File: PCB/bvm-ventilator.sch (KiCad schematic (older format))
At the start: 6 parts, among them U1 IEC_CONNECTOR

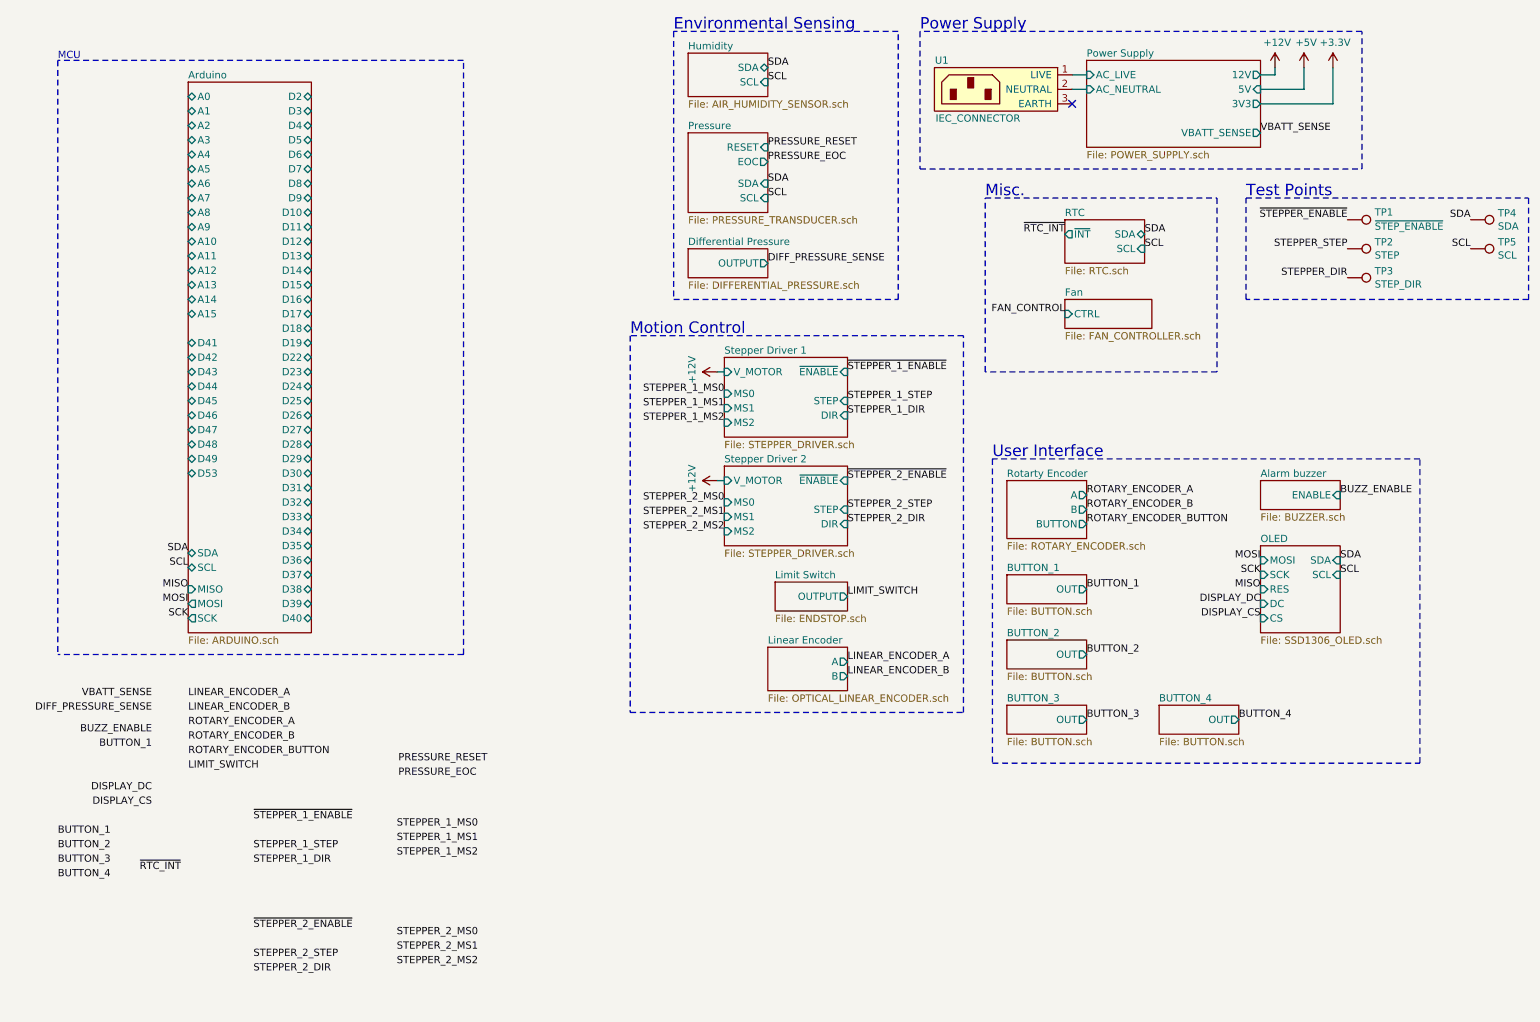
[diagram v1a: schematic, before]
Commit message: Added TFT Display sheet
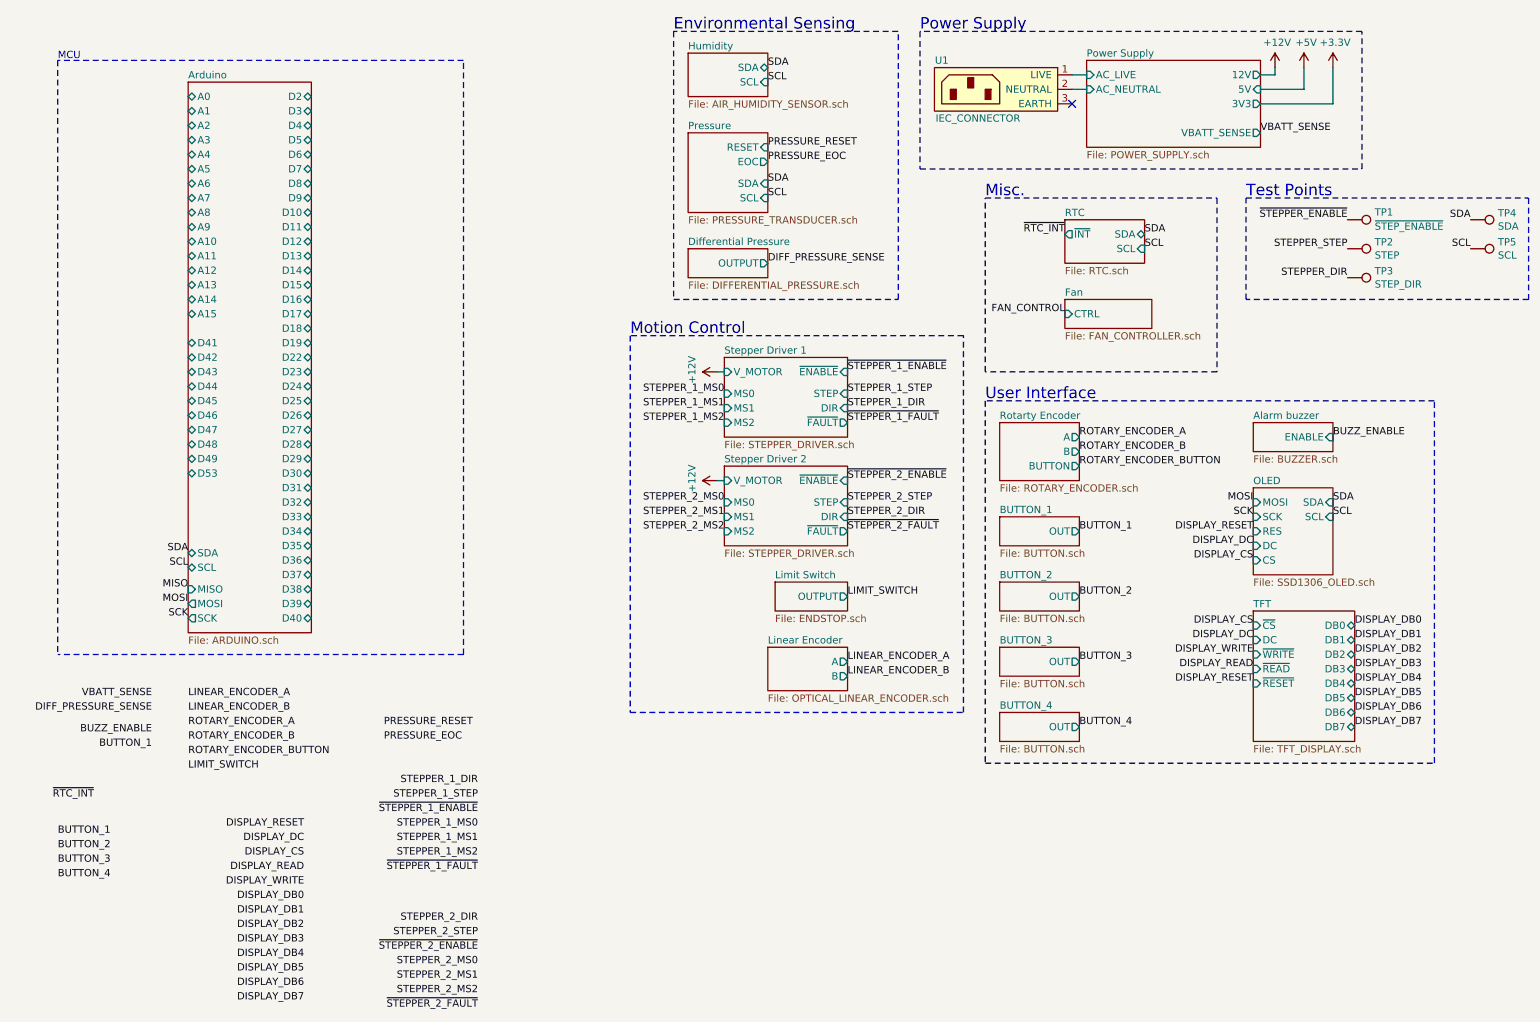
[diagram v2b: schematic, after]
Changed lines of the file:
@@
 $Descr A4 11693 8268
 encoding utf-8
-Sheet 1 26
+Sheet 1 27
 Title "ResQVenT"
 Date ""
@@
 F1 "STEPPER_DRIVER.sch" 50
 F2 "V_MOTOR" I L 5450 3150 50
-F3 "STEP" I R 6300 3350 50
-F4 "DIR" I R 6300 3450 50
+F3 "STEP" I R 6300 3300 50
+F4 "DIR" I R 6300 3400 50
 F5 "~ENABLE" I R 6300 3150 50
 F6 "MS0" I L 5450 3300 50
 F7 "MS1" I L 5450 3400 50
 F8 "MS2" I L 5450 3500 50
-$EndSheet
-$Sheet
-S 9150 3900 550  200
+F9 "~FAULT" O R 6300 3500 50
+$EndSheet
+$Sheet
+S 9100 3500 550  200
 U 5E8EB699
 F0 "Alarm buzzer" 50
 F1 "BUZZER.sch" 50
-F2 "ENABLE" I R 9700 4000 50
-$EndSheet
-$Sheet
-S 9150 4350 550  600
+F2 "ENABLE" I R 9650 3600 50
+$EndSheet
+$Sheet
+S 9100 3950 550  600
 U 5E8F3A13
 F0 "OLED" 50
 F1 "SSD1306_OLED.sch" 50
-F2 "SCL" I R 9700 4550 50
-F3 "SDA" I R 9700 4450 50
-F4 "MOSI" I L 9150 4450 50
-F5 "SCK" I L 9150 4550 50
-F6 "DC" I L 9150 4750 50
-F7 "CS" I L 9150 4850 50
-F8 "RES" I L 9150 4650 50
+F2 "SCL" I R 9650 4150 50
+F3 "SDA" I R 9650 4050 50
+F4 "MOSI" I L 9100 4050 50
+F5 "SCK" I L 9100 4150 50
+F6 "DC" I L 9100 4350 50
+F7 "CS" I L 9100 4450 50
+F8 "RES" I L 9100 4250 50
 $EndSheet
 $Sheet
@@
 F1 "STEPPER_DRIVER.sch" 50
 F2 "V_MOTOR" I L 5450 3900 50
-F3 "STEP" I R 6300 4100 50
-F4 "DIR" I R 6300 4200 50
+F3 "STEP" I R 6300 4050 50
+F4 "DIR" I R 6300 4150 50
 F5 "~ENABLE" I R 6300 3900 50
 F6 "MS0" I L 5450 4050 50
 F7 "MS1" I L 5450 4150 50
 F8 "MS2" I L 5450 4250 50
+F9 "~FAULT" O R 6300 4250 50
 $EndSheet
 $Sheet
@@
 Text Label 1750 4500 2    50   ~ 0
 SCL
-Text Label 9700 4450 0    50   ~ 0
+Text Label 9650 4050 0    50   ~ 0
 SDA
-Text Label 9700 4550 0    50   ~ 0
+Text Label 9650 4150 0    50   ~ 0
 SCL
 Text Label 5750 1850 0    50   ~ 0
@@
 Text Label 8350 2300 0    50   ~ 0
 SCL
-Text Label 6300 3350 0    50   ~ 0
+Text Label 6300 3300 0    50   ~ 0
 STEPPER_1_STEP
-Text Label 6300 3450 0    50   ~ 0
+Text Label 6300 3400 0    50   ~ 0
 STEPPER_1_DIR
-Text Label 6300 4100 0    50   ~ 0
+Text Label 6300 4050 0    50   ~ 0
 STEPPER_2_STEP
-Text Label 6300 4200 0    50   ~ 0
+Text Label 6300 4150 0    50   ~ 0
 STEPPER_2_DIR
-Text Label 9700 4000 0    50   ~ 0
+Text Label 9650 3600 0    50   ~ 0
 BUZZ_ENABLE
-Text Label 1500 5650 2    50   ~ 0
-BUZZ_ENABLE
-Text Label 1750 5900 0    50   ~ 0
-LIMIT_SWITCH
 Text Label 6300 4700 0    50   ~ 0
 LIMIT_SWITCH
@@
 VBATT_SENSE
 $Sheet
-S 7400 3900 550  400
+S 7350 3500 550  400
 U 5E8BEE14
 F0 "Rotarty Encoder" 50
 F1 "ROTARY_ENCODER.sch" 50
-F2 "A" O R 7950 4000 50
-F3 "B" O R 7950 4100 50
-F4 "BUTTON" O R 7950 4200 50
-$EndSheet
-Text Label 7950 4000 0    50   ~ 0
+F2 "A" O R 7900 3600 50
+F3 "B" O R 7900 3700 50
+F4 "BUTTON" O R 7900 3800 50
+$EndSheet
+Text Label 7900 3600 0    50   ~ 0
 ROTARY_ENCODER_A
-Text Label 7950 4100 0    50   ~ 0
+Text Label 7900 3700 0    50   ~ 0
 ROTARY_ENCODER_B
-Text Label 7950 4200 0    50   ~ 0
+Text Label 7900 3800 0    50   ~ 0
 ROTARY_ENCODER_BUTTON
-Text Label 1750 5600 0    50   ~ 0
-ROTARY_ENCODER_A
-Text Label 1750 5700 0    50   ~ 0
-ROTARY_ENCODER_B
-Text Label 1750 5800 0    50   ~ 0
-ROTARY_ENCODER_BUTTON
-$Sheet
-S 7400 4550 550  200
+$Sheet
+S 7350 4150 550  200
 U 5E8CBD7F
 F0 "BUTTON_1" 50
 F1 "BUTTON.sch" 50
-F2 "OUT" O R 7950 4650 50
-$EndSheet
-Text Label 7950 4650 0    50   ~ 0
-BUTTON_1
-Text Label 1500 5750 2    50   ~ 0
+F2 "OUT" O R 7900 4250 50
+$EndSheet
+Text Label 7900 4250 0    50   ~ 0
 BUTTON_1
 Text Label 6300 3150 0    50   ~ 0
@@
 Text Label 6300 5250 0    50   ~ 0
 LINEAR_ENCODER_B
-Text Label 1750 5400 0    50   ~ 0
-LINEAR_ENCODER_A
-Text Label 1750 5500 0    50   ~ 0
-LINEAR_ENCODER_B
 $Sheet
 S 5200 950  550  300
@@
 Text Label 1750 4850 2    50   ~ 0
 SCK
-Text Label 9150 4750 2    50   ~ 0
+Text Label 9100 4350 2    50   ~ 0
 DISPLAY_DC
-Text Label 9150 4850 2    50   ~ 0
+Text Label 9100 4450 2    50   ~ 0
 DISPLAY_CS
-Text Label 9150 4650 2    50   ~ 0
-MISO
-Text Label 9150 4450 2    50   ~ 0
+Text Label 9100 4050 2    50   ~ 0
 MOSI
-Text Label 9150 4550 2    50   ~ 0
+Text Label 9100 4150 2    50   ~ 0
 SCK
 Wire Notes Line
-	7300 3750 7300 5850
-Wire Notes Line
-	7300 5850 10250 5850
-Wire Notes Line
-	10250 5850 10250 3750
-Wire Notes Line
-	10250 3750 7300 3750
+	7250 3350 7250 5850
+Wire Notes Line
+	7250 5850 10350 5850
+Wire Notes Line
+	10350 3350 7250 3350
 Text Notes 4800 2900 0    79   ~ 0
 Motion Control
@@
 Text Notes 5100 800  0    79   ~ 0
 Environmental Sensing
-Text Notes 7300 3750 0    79   ~ 0
+Text Notes 7250 3350 0    79   ~ 0
 User Interface
 Wire Wire Line
@@
 Text Label 7800 2200 2    50   ~ 0
 ~RTC_INT
-Text Label 1700 6600 2    50   ~ 0
+Text Label 1100 6100 2    50   ~ 0
 ~RTC_INT
-Text Label 2200 6450 0    50   ~ 0
-STEPPER_1_STEP
-Text Label 2200 6550 0    50   ~ 0
-STEPPER_1_DIR
-Text Label 2200 7200 0    50   ~ 0
-STEPPER_2_STEP
-Text Label 2200 7300 0    50   ~ 0
-STEPPER_2_DIR
-Text Label 2200 7000 0    50   ~ 0
-~STEPPER_2_ENABLE
-Text Label 2200 6250 0    50   ~ 0
-~STEPPER_1_ENABLE
 Text Label 5450 3300 2    50   ~ 0
 STEPPER_1_MS0
@@
 Text Label 5450 4250 2    50   ~ 0
 STEPPER_2_MS2
-Text Label 3750 6300 2    50   ~ 0
-STEPPER_1_MS0
-Text Label 3750 6400 2    50   ~ 0
-STEPPER_1_MS1
-Text Label 3750 6500 2    50   ~ 0
-STEPPER_1_MS2
-Text Label 3750 7050 2    50   ~ 0
-STEPPER_2_MS0
-Text Label 3750 7150 2    50   ~ 0
-STEPPER_2_MS1
-Text Label 3750 7250 2    50   ~ 0
-STEPPER_2_MS2
 Text Label 5750 1600 0    50   ~ 0
 PRESSURE_RESET
 Text Label 5750 1700 0    50   ~ 0
 PRESSURE_EOC
-Text Label 3200 5850 0    50   ~ 0
-PRESSURE_RESET
-Text Label 3200 5950 0    50   ~ 0
-PRESSURE_EOC
-$Sheet
-S 7400 5000 550  200
+$Sheet
+S 7350 4600 550  200
 U 5E96853E
 F0 "BUTTON_2" 50
 F1 "BUTTON.sch" 50
-F2 "OUT" O R 7950 5100 50
-$EndSheet
-Text Label 7950 5100 0    50   ~ 0
+F2 "OUT" O R 7900 4700 50
+$EndSheet
+Text Label 7900 4700 0    50   ~ 0
 BUTTON_2
 $Sheet
-S 7400 5450 550  200
+S 7350 5050 550  200
 U 5E968934
 F0 "BUTTON_3" 50
 F1 "BUTTON.sch" 50
-F2 "OUT" O R 7950 5550 50
-$EndSheet
-Text Label 7950 5550 0    50   ~ 0
+F2 "OUT" O R 7900 5150 50
+$EndSheet
+Text Label 7900 5150 0    50   ~ 0
 BUTTON_3
 $Sheet
-S 8450 5450 550  200
+S 7350 5500 550  200
 U 5E968D0C
 F0 "BUTTON_4" 50
 F1 "BUTTON.sch" 50
-F2 "OUT" O R 9000 5550 50
-$EndSheet
-Text Label 9000 5550 0    50   ~ 0
+F2 "OUT" O R 7900 5600 50
+$EndSheet
+Text Label 7900 5600 0    50   ~ 0
 BUTTON_4
 Text Label 850  6450 0    50   ~ 0
@@
 Text Label 850  6350 0    50   ~ 0
 BUTTON_1
-Text Label 1500 6050 2    50   ~ 0
+Text Label 2550 6400 2    50   ~ 0
 DISPLAY_DC
-Text Label 1500 6150 2    50   ~ 0
+Text Label 2550 6500 2    50   ~ 0
 DISPLAY_CS
+Text Label 6300 3500 0    50   ~ 0
+~STEPPER_1_FAULT
+Text Label 6300 4250 0    50   ~ 0
+~STEPPER_2_FAULT
+Text Label 1500 5650 2    50   ~ 0
+BUZZ_ENABLE
+Text Label 1500 5750 2    50   ~ 0
+BUTTON_1
+Text Label 1750 5500 0    50   ~ 0
+LINEAR_ENCODER_B
+Text Label 1750 5400 0    50   ~ 0
+LINEAR_ENCODER_A
+Text Label 1750 5800 0    50   ~ 0
+ROTARY_ENCODER_BUTTON
+Text Label 1750 5700 0    50   ~ 0
+ROTARY_ENCODER_B
+Text Label 1750 5600 0    50   ~ 0
+ROTARY_ENCODER_A
+Text Label 1750 5900 0    50   ~ 0
+LIMIT_SWITCH
+Text Label 3100 5700 0    50   ~ 0
+PRESSURE_EOC
+Text Label 3100 5600 0    50   ~ 0
+PRESSURE_RESET
+Text Label 3750 6600 2    50   ~ 0
+~STEPPER_1_FAULT
+Text Label 3750 6500 2    50   ~ 0
+STEPPER_1_MS2
+Text Label 3750 6400 2    50   ~ 0
+STEPPER_1_MS1
+Text Label 3750 6300 2    50   ~ 0
+STEPPER_1_MS0
+Text Label 3750 6200 2    50   ~ 0
+~STEPPER_1_ENABLE
+Text Label 3750 6000 2    50   ~ 0
+STEPPER_1_DIR
+Text Label 3750 6100 2    50   ~ 0
+STEPPER_1_STEP
+Text Label 3750 7050 2    50   ~ 0
+STEPPER_2_STEP
+Text Label 3750 6950 2    50   ~ 0
+STEPPER_2_DIR
+Text Label 3750 7550 2    50   ~ 0
+~STEPPER_2_FAULT
+Text Label 3750 7450 2    50   ~ 0
+STEPPER_2_MS2
+Text Label 3750 7350 2    50   ~ 0
+STEPPER_2_MS1
+Text Label 3750 7250 2    50   ~ 0
+STEPPER_2_MS0
+Text Label 3750 7150 2    50   ~ 0
+~STEPPER_2_ENABLE
+Text Label 9100 4250 2    50   ~ 0
+DISPLAY_RESET
+$Sheet
+S 9100 4800 700  900
+U 5E97D98A
+F0 "TFT" 50
+F1 "TFT_DISPLAY.sch" 50
+F2 "~CS" I L 9100 4900 50
+F3 "DC" I L 9100 5000 50
+F4 "~WRITE" I L 9100 5100 50
+F5 "~READ" I L 9100 5200 50
+F6 "~RESET" I L 9100 5300 50
+F7 "DB0" B R 9800 4900 50
+F8 "DB1" B R 9800 5000 50
+F9 "DB2" B R 9800 5100 50
+F10 "DB3" B R 9800 5200 50
+F11 "DB4" B R 9800 5300 50
+F12 "DB5" B R 9800 5400 50
+F13 "DB6" B R 9800 5500 50
+F14 "DB7" B R 9800 5600 50
+$EndSheet
+Text Label 2550 6300 2    50   ~ 0
+DISPLAY_RESET
+Text Label 2550 6600 2    50   ~ 0
+DISPLAY_READ
+Text Label 2550 6700 2    50   ~ 0
+DISPLAY_WRITE
+Text Label 9100 5000 2    50   ~ 0
+DISPLAY_DC
+Text Label 9100 4900 2    50   ~ 0
+DISPLAY_CS
+Text Label 9100 5300 2    50   ~ 0
+DISPLAY_RESET
+Text Label 9100 5200 2    50   ~ 0
+DISPLAY_READ
+Text Label 9100 5100 2    50   ~ 0
+DISPLAY_WRITE
+Text Label 9800 4900 0    50   ~ 0
+DISPLAY_DB0
+Text Label 9800 5000 0    50   ~ 0
+DISPLAY_DB1
+Text Label 9800 5100 0    50   ~ 0
+DISPLAY_DB2
+Text Label 9800 5200 0    50   ~ 0
+DISPLAY_DB3
+Text Label 9800 5300 0    50   ~ 0
+DISPLAY_DB4
+Text Label 9800 5400 0    50   ~ 0
+DISPLAY_DB5
+Text Label 9800 5500 0    50   ~ 0
+DISPLAY_DB6
+Text Label 9800 5600 0    50   ~ 0
+DISPLAY_DB7
+Text Label 2550 6800 2    50   ~ 0
+DISPLAY_DB0
+Text Label 2550 6900 2    50   ~ 0
+DISPLAY_DB1
+Text Label 2550 7000 2    50   ~ 0
+DISPLAY_DB2
+Text Label 2550 7100 2    50   ~ 0
+DISPLAY_DB3
+Text Label 2550 7200 2    50   ~ 0
+DISPLAY_DB4
+Text Label 2550 7300 2    50   ~ 0
+DISPLAY_DB5
+Text Label 2550 7400 2    50   ~ 0
+DISPLAY_DB6
+Text Label 2550 7500 2    50   ~ 0
+DISPLAY_DB7
+Wire Notes Line
+	10350 5850 10350 3350
 $EndSCHEMATC

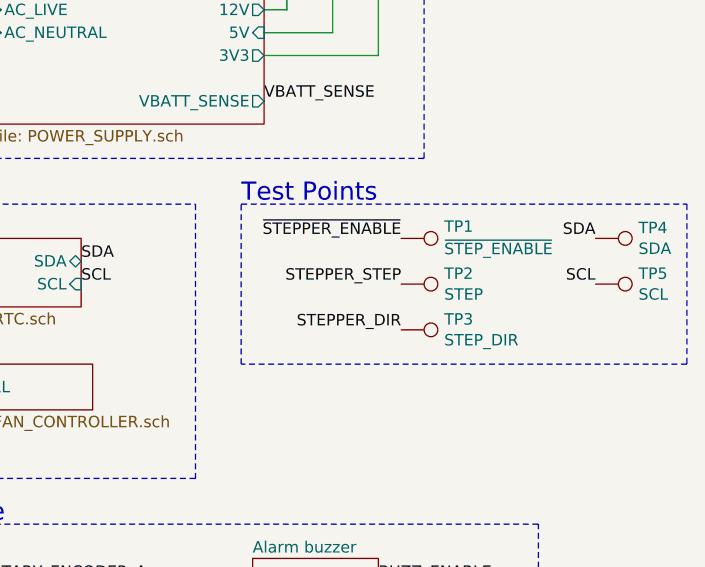
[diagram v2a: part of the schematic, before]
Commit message: Removed unused testpoints
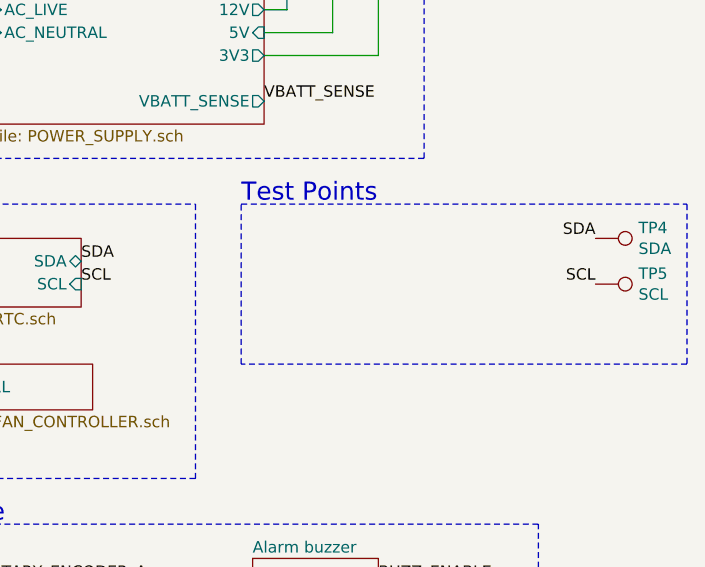
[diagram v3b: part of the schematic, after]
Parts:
- removed TP1: ~STEP_ENABLE, custom:TestPoint_Pad_D1.5mm, symbol Connector:TestPoint
- removed TP2: STEP, custom:TestPoint_Pad_D1.5mm, symbol Connector:TestPoint
- removed TP3: STEP_DIR, custom:TestPoint_Pad_D1.5mm, symbol Connector:TestPoint
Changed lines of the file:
@@
 Text Label 10600 2300 2    50   ~ 0
 SCL
-Text Label 9750 2300 2    50   ~ 0
-STEPPER_STEP
-Text Label 9750 2500 2    50   ~ 0
-STEPPER_DIR
-Text Label 9750 2100 2    50   ~ 0
-~STEPPER_ENABLE
-$Comp
-L Connector:TestPoint TP1
-U 1 1 5E9B874A
-P 9750 2100
-F 0 "TP1" V 9698 2288 50  0000 L CNN
-F 1 "~STEP_ENABLE" V 9796 2288 50  0000 L CNN
-F 2 "custom:TestPoint_Pad_D1.5mm" H 9950 2100 50  0001 C CNN
-F 3 "~" H 9950 2100 50  0001 C CNN
-	1    9750 2100
-	0    1    1    0
-$EndComp
-$Comp
-L Connector:TestPoint TP2
-U 1 1 5E9B88D9
-P 9750 2300
-F 0 "TP2" V 9704 2488 50  0000 L CNN
-F 1 "STEP" V 9795 2488 50  0000 L CNN
-F 2 "custom:TestPoint_Pad_D1.5mm" H 9950 2300 50  0001 C CNN
-F 3 "~" H 9950 2300 50  0001 C CNN
-	1    9750 2300
-	0    1    1    0
-$EndComp
-$Comp
-L Connector:TestPoint TP3
-U 1 1 5E9B8AC5
-P 9750 2500
-F 0 "TP3" V 9704 2688 50  0000 L CNN
-F 1 "STEP_DIR" V 9795 2688 50  0000 L CNN
-F 2 "custom:TestPoint_Pad_D1.5mm" H 9950 2500 50  0001 C CNN
-F 3 "~" H 9950 2500 50  0001 C CNN
-	1    9750 2500
-	0    1    1    0
-$EndComp
 $Comp
 L Connector:TestPoint TP4
